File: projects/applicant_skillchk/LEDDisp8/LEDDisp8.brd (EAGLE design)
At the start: 83.8 x 100 mm, 30 parts, among them J1 4X2, J2 3X1A

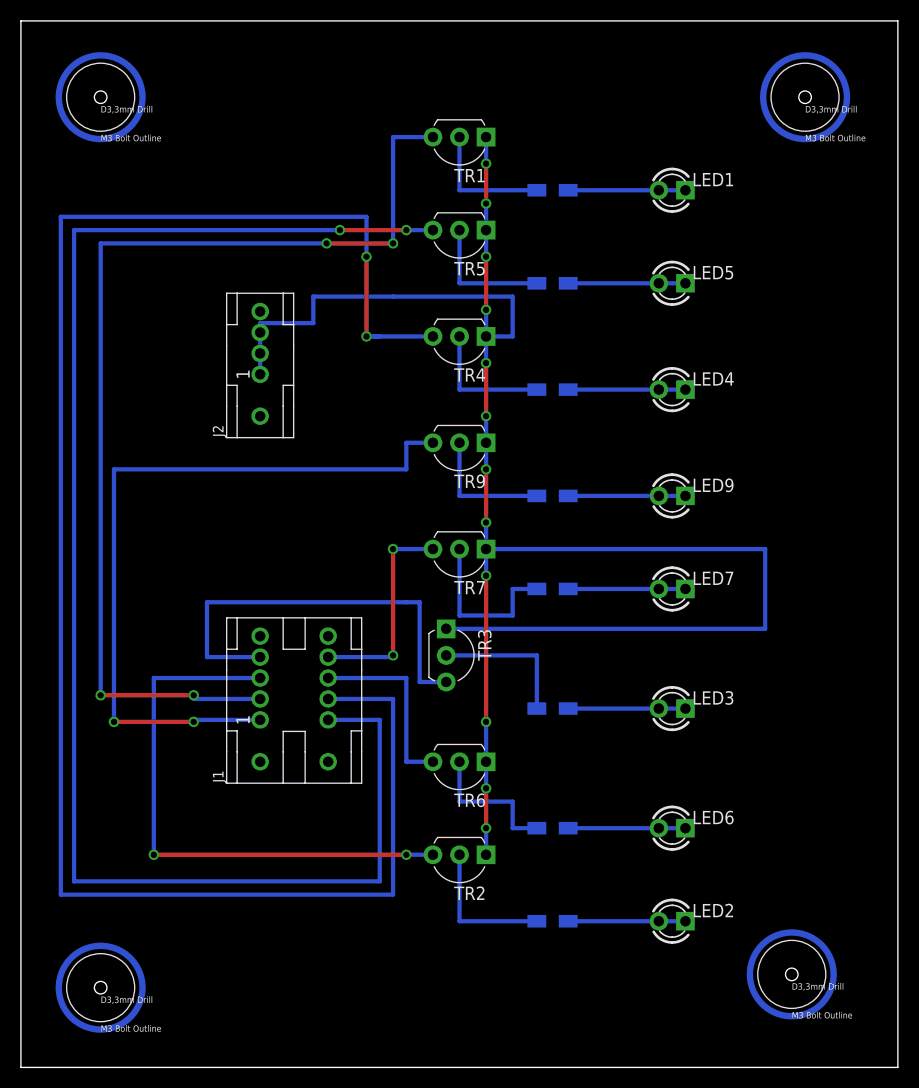
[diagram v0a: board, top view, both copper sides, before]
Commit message: 回路図の修正
DRCのエラーの修正
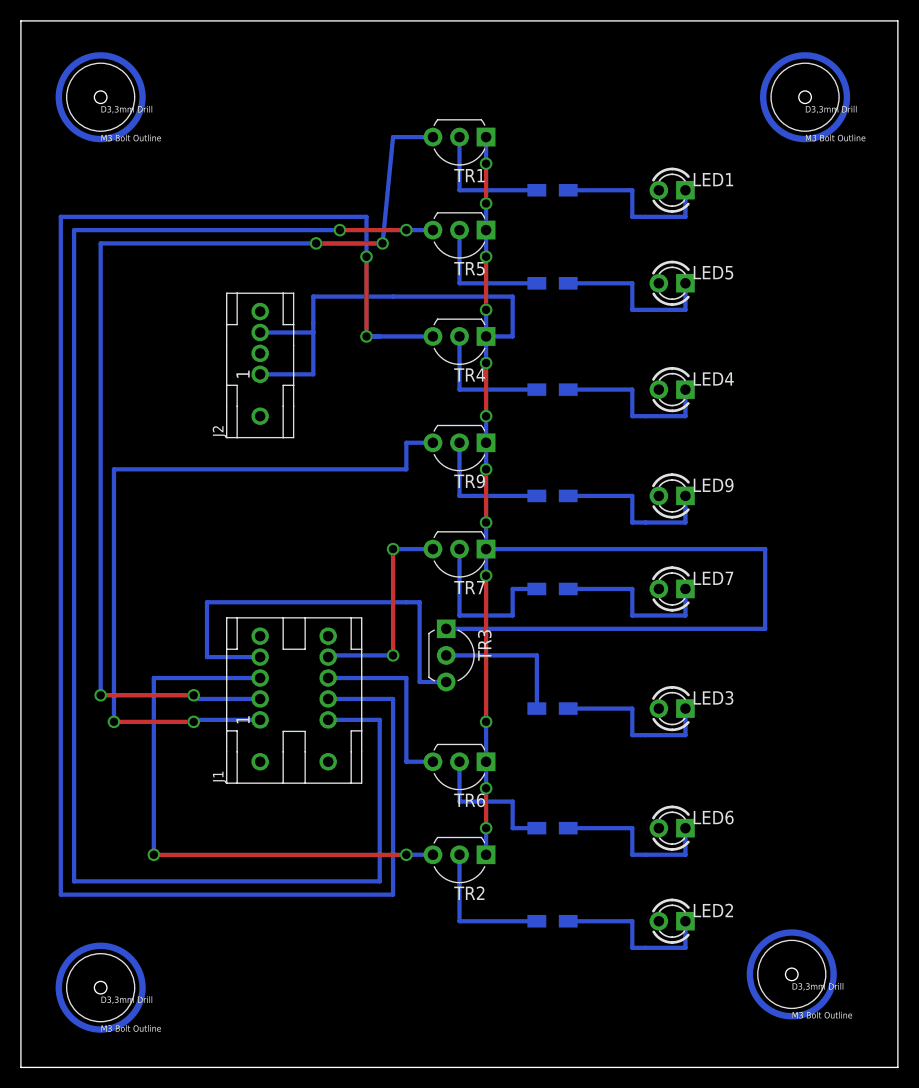
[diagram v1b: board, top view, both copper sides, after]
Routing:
- net N$26: track 11.2 -> 16.3 mm
- net N$21: track 11.2 -> 16.3 mm
- net N$5: track 11.2 -> 16.3 mm
- net N$25: track 11.2 -> 16.3 mm
- net N$24: track 11.2 -> 16.3 mm
- net N$23: track 11.2 -> 16.3 mm
- net N$22: track 11.2 -> 16.3 mm
- net N$19: track 11.2 -> 16.3 mm
- net GND: track 171.3 -> 176.3 mm
- net P2: track 100.7 -> 99.7 mm
